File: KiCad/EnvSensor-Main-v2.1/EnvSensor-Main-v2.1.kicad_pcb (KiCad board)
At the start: 4 copper layers, 102 x 100 mm, 90 parts, among them J1 Conn_01x02, J2 Conn_01x02, J3 HPMA115C0-003, J4 Conn_01x02, J5 Micro_SD_Card_Det, J6 SWD, J7 I2C, J8 POWER_INPUT, Q1 Si3407DV, Q2 IRLML2502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

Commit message: Finishing touches
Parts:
- moved JP4 2.87 mm to (40.6, 81.1)
- moved J4 1.65 mm to (38.1, 79.7)
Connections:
- net Net-(J2-Pin_1) renamed /SCD_POWER
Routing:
- net +3V3: track 327.9 -> 320.2 mm, vias 17 -> 15
- net SDIO_CLK: track 47.9 -> 49.4 mm
- net WIFI_ENABLE: track 69.8 -> 68.9 mm
- net Net-(R10-Pad2): track 72.9 -> 72.3 mm
- net POWER_5V_ENABLE: track 94.6 -> 95.2 mm
- net SDIO_DATA0: track 35.7 -> 35.1 mm
- net GND: vias 77 -> 79

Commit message: More fixes
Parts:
- C25: footprint Capacitor_SMD:CP_Elec_6.3x5.8 -> Capacitor_SMD:CP_Elec_4x5.3
- J7: footprint Connector_PinSocket_2.54mm:PinSocket_1x04_P2.54mm_Vertical -> Connector_PinSocket_2.54mm:PinSocket_1x04_P2.54mm_Horizontal; moved to B.Cu
- moved D3 17.0 mm to (106.8, 111.7)
- moved D4 17.0 mm to (108.0, 110.0)
- moved R19 17.0 mm to (106.8, 107.7)
- moved D7 11.2 mm to (98.8, 111.8)
- moved D8 11.2 mm to (100.0, 110.0)
- moved R21 11.2 mm to (98.8, 107.8)
- moved D1 9.50 mm to (90.8, 111.7)
- moved D2 9.50 mm to (92.0, 110.0)
- moved R18 9.50 mm to (90.8, 107.7)
- moved D5 6.95 mm to (82.7, 111.7)
- moved D6 6.95 mm to (84.0, 110.0)
- moved R20 6.95 mm to (82.8, 107.7)
- moved J7 5.65 mm to (80.9, 29.4), turned to -90 degrees
- moved J8 1.69 mm to (111.0, 115.0)
- moved U7 1.22 mm to (19.5, 107.5)
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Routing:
- net LED_2: track 90.1 -> 107.4 mm
- net LED_1: track 87.1 -> 94.7 mm
- net SDA: track 156.5 -> 150.9 mm
- net SCL: track 153.3 -> 147.8 mm
- net LED_4: track 97.4 -> 101.3 mm
- net LED_3: track 94.4 -> 91.0 mm
- net +5V: track 148.0 -> 149.9 mm
- net POWER_5V_ENABLE: track 95.2 -> 96.7 mm
- net GND: track 149.2 -> 148.1 mm, vias 79 -> 80
- net +3V3: track 320.2 -> 319.5 mm
- net E_INK_SELECT: track 27.5 -> 28.1 mm
- net E_INK_RESET: track 29.2 -> 29.7 mm
- net E_INK_BUSY: track 30.1 -> 30.6 mm
- net SCK: track 27.1 -> 27.6 mm
- net E_INK_DC: track 28.4 -> 28.9 mm

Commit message: More fixes
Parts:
- added H5: MountingHole, TestPoint:TestPoint_THTPad_D1.5mm_Drill0.7mm, F.Cu at (78.8, 23.6)
- added H6: MountingHole, TestPoint:TestPoint_THTPad_D1.5mm_Drill0.7mm, F.Cu at (92.8, 23.6)
- J7: moved to F.Cu
- L1: footprint Inductor_SMD:L_1206_3216Metric -> Inductor_SMD:L_1210_3225Metric
- Q1: footprint Package_TO_SOT_SMD:TSOT-23-6 -> Package_TO_SOT_SMD:TSOT-23-6_HandSoldering
- Q2: footprint Package_TO_SOT_SMD:SOT-23 -> Package_TO_SOT_SMD:SOT-23-3
- SW1: footprint Button_Switch_THT:SW_Tactile_SKHH_Angled -> Button_Switch_THT:SW_Tactile_SPST_Angled_PTS645Vx83-2LFS
- moved J7 8.80 mm to (89.6, 28.4)
- moved J5 3.29 mm to (28.5, 93.0)
- moved D2 2.28 mm to (92.0, 112.3), turned to 90 degrees
- moved D8 2.28 mm to (100.0, 112.3), turned to 90 degrees
- moved D4 2.20 mm to (108.0, 112.2), turned to 90 degrees
- moved D6 2.20 mm to (84.0, 112.2), turned to 90 degrees
- moved SW1 1.83 mm to (21.7, 46.1)
- moved D1 1.53 mm to (89.6, 110.8), turned to 90 degrees
- moved D7 1.49 mm to (97.6, 110.8), turned to 90 degrees
- moved D3 1.47 mm to (105.6, 110.8), turned to 90 degrees
- moved D5 1.42 mm to (81.6, 110.8), turned to 90 degrees
- moved R21 1.20 mm to (99.1, 106.6), turned to 0 degrees
- moved R18 1.17 mm to (91.1, 106.6), turned to 0 degrees
- moved R19 1.16 mm to (107.1, 106.6), turned to 0 degrees
- moved R20 1.16 mm to (83.1, 106.6), turned to 0 degrees
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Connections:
- D1 pad 1: Net-(D1-K) -> GND
- D1 pad 2: LED_1 -> Net-(D1-A)
- D2 pad 1: Net-(D1-K) -> GND
- D2 pad 2: LED_1 -> Net-(D1-A)
- D3 pad 1: Net-(D3-K) -> GND
- D3 pad 2: LED_2 -> Net-(D3-A)
- D4 pad 1: Net-(D3-K) -> GND
- D4 pad 2: LED_2 -> Net-(D3-A)
- D5 pad 1: Net-(D5-K) -> GND
- D5 pad 2: LED_3 -> Net-(D5-A)
- D6 pad 1: Net-(D5-K) -> GND
- D6 pad 2: LED_3 -> Net-(D5-A)
- D7 pad 1: Net-(D7-K) -> GND
- D7 pad 2: LED_4 -> Net-(D7-A)
- D8 pad 1: Net-(D7-K) -> GND
- D8 pad 2: LED_4 -> Net-(D7-A)
- R18 pad 1: Net-(D1-K) -> LED_1
- R18 pad 2: GND -> Net-(D1-A)
- R19 pad 1: Net-(D3-K) -> LED_2
- R19 pad 2: GND -> Net-(D3-A)
- R20 pad 1: Net-(D5-K) -> LED_3
- R20 pad 2: GND -> Net-(D5-A)
- R21 pad 1: Net-(D7-K) -> LED_4
- R21 pad 2: GND -> Net-(D7-A)
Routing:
- net +3V3: track 319.5 -> 300.2 mm
- net GND: track 148.1 -> 157.8 mm, vias 80 -> 76
- net LED_3: track 91.0 -> 83.2 mm
- net LED_1: track 94.7 -> 88.6 mm
- net LED_4: track 101.3 -> 95.4 mm
- net Net-(D7-A): track 0.00 -> 5.59 mm
- net Net-(D1-A): track 0.00 -> 5.59 mm
- net Net-(D5-A): track 0.00 -> 5.54 mm
- net Net-(D3-A): track 0.00 -> 5.54 mm
- net LED_2: track 107.4 -> 102.2 mm
- net Net-(D5-K): track 4.30 -> 0.00 mm
- net Net-(D7-K): track 4.27 -> 0.00 mm
- net Net-(D3-K): track 4.27 -> 0.00 mm
- net Net-(D1-K): track 4.24 -> 0.00 mm
- net POWER_5V_ENABLE: track 96.7 -> 100.0 mm
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
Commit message: More work
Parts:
- J1, J2, J4: footprint Connector_PinHeader_2.54mm:PinHeader_1x02_P2.54mm_Vertical -> Connector_PinHeader_2.54mm:PinHeader_1x02_P2.54mm_Horizontal
- moved R9 19.4 mm to (64.8, 68.2), turned to 0 degrees
- moved R8 17.8 mm to (69.1, 68.0), turned to 180 degrees
- moved JP4 7.77 mm to (33.4, 83.8), turned to 0 degrees
- moved J4 6.27 mm to (32.1, 81.4), turned to 90 degrees
- moved JP2 4.01 mm to (93.2, 47.0), turned to 180 degrees
- moved R3 3.30 mm to (41.1, 86.5)
- moved R4 3.30 mm to (41.1, 88.5)
- moved C14 3.30 mm to (40.0, 91.3)
- moved C15 3.30 mm to (41.7, 91.2)
- moved Q1 3.30 mm to (41.0, 83.2)
- moved R2 3.30 mm to (41.0, 80.5)
- moved R5 3.30 mm to (43.0, 95.8)
- moved R6 3.30 mm to (41.0, 96.6)
- moved R7 3.30 mm to (39.0, 97.2)
- moved L1 0.45 mm to (44.2, 46.6)
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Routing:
- net +3V3: track 300.2 -> 314.2 mm, vias 15 -> 14
- net SCL: track 147.8 -> 155.9 mm
- net SDIO_DETECT: track 40.3 -> 36.7 mm
- net SDIO_POWER_ENABLE: track 32.3 -> 29.1 mm
- net +3.3VA: track 5.02 -> 7.91 mm
- net Net-(J4-Pin_2): track 7.33 -> 9.22 mm
- net SDIO_DATA1: track 33.2 -> 34.6 mm
- net SDIO_DATA0: track 35.1 -> 36.5 mm
- net POWER_5V_ENABLE: track 100.0 -> 98.6 mm
- net LED_3: track 83.2 -> 82.1 mm
- net LED_1: track 88.6 -> 87.5 mm
- net SDIO_CMD: track 55.4 -> 54.5 mm
- net SDIO_DATA3: track 52.1 -> 51.2 mm
- net LED_4: track 95.4 -> 94.6 mm
- net LED_2: track 102.2 -> 101.4 mm
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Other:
- board text added: "5V En"
- board text added: "NRST"
- board text added: "SWCLK"
- board text added: "SWDIO"
- board text added: "SWO"
- board text removed: "5V Enable"

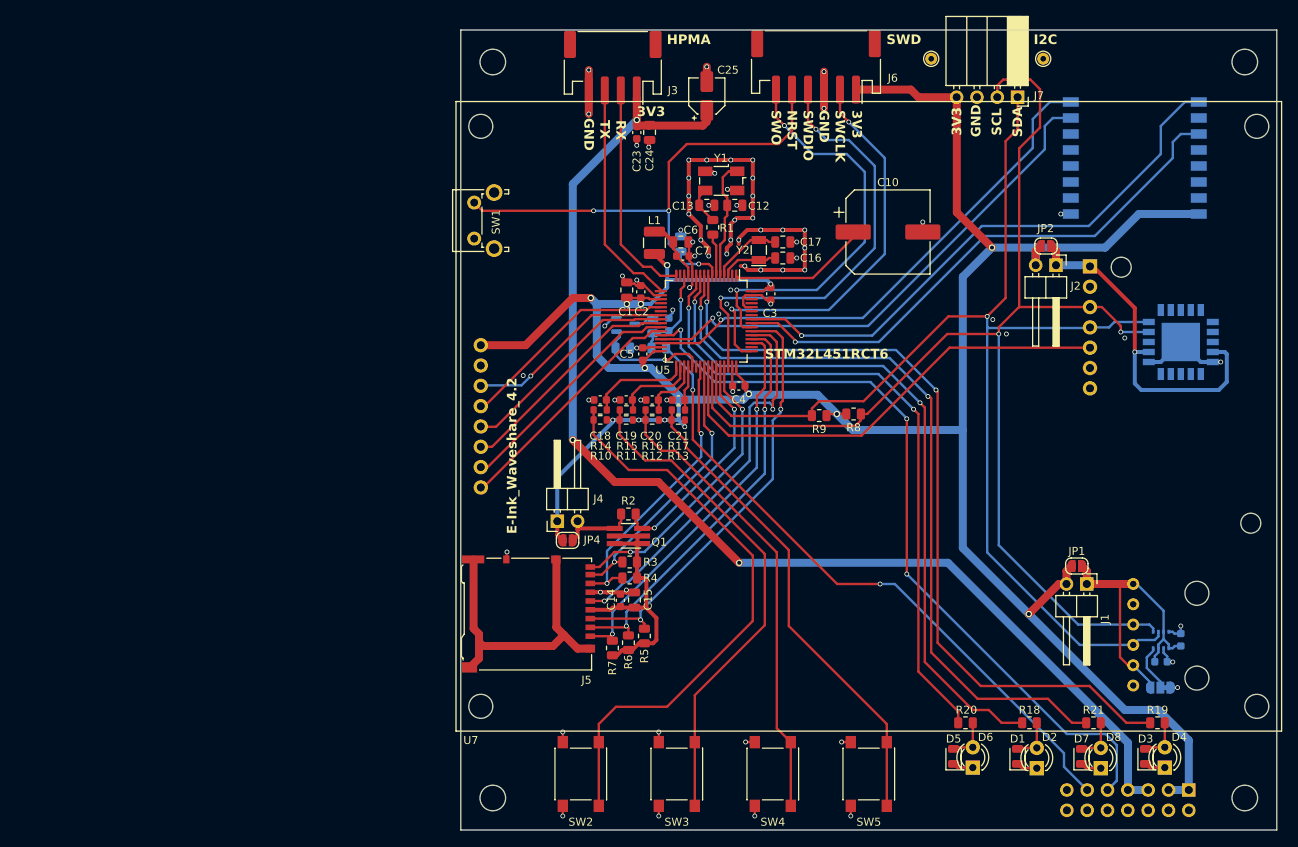
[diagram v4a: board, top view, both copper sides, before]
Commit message: Bore moving swd and i2c
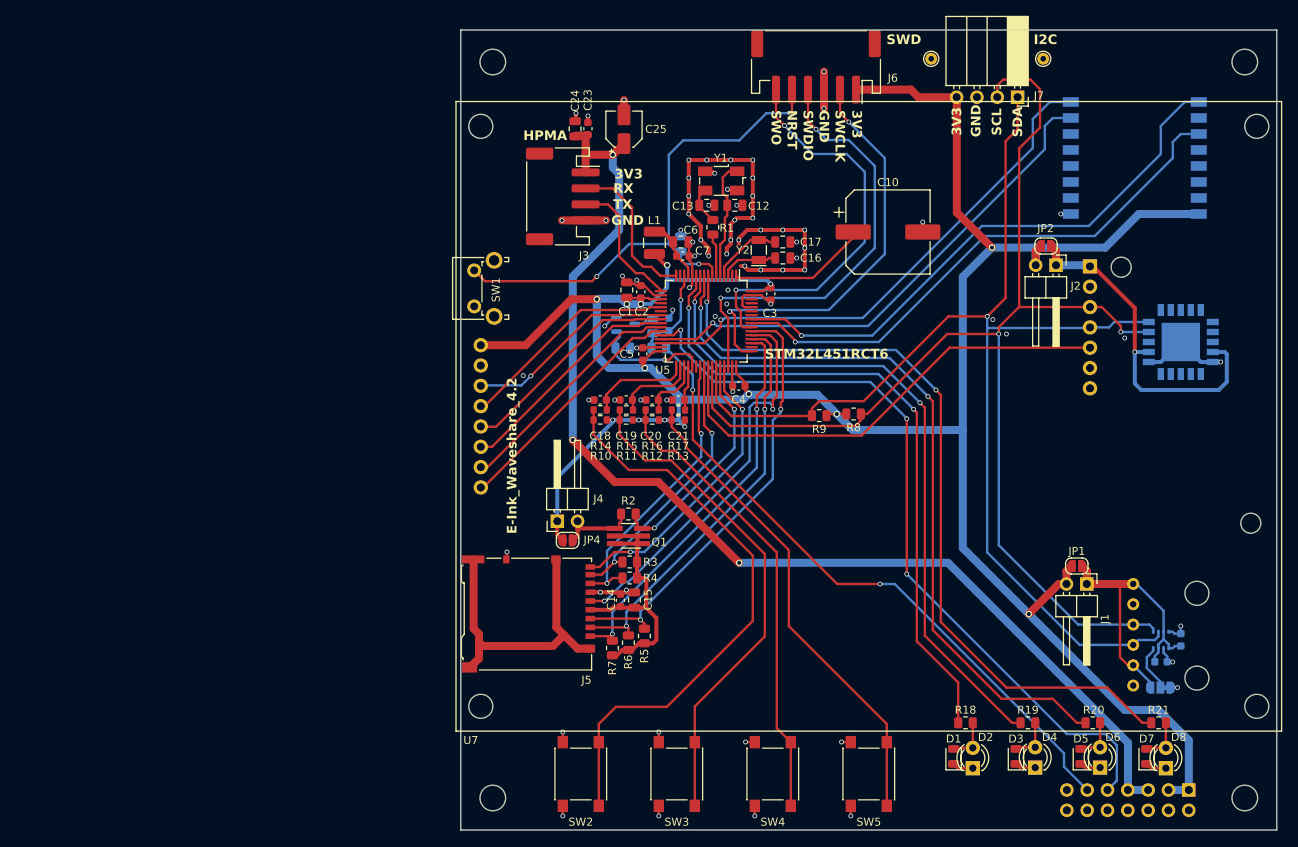
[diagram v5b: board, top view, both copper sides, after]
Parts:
- moved J3 17.3 mm to (32.8, 40.8), turned to -90 degrees
- moved D4 16.2 mm to (91.8, 112.2)
- moved R19 16.2 mm to (90.9, 106.6)
- moved D3 16.2 mm to (89.4, 110.8)
- moved D5 15.9 mm to (97.5, 110.8)
- moved D6 15.9 mm to (99.9, 112.2)
- moved R20 15.9 mm to (99.0, 106.6)
- moved C25 11.2 mm to (40.4, 32.4)
- moved C24 9.32 mm to (34.3, 32.4), turned to 90 degrees
- moved SW1 8.47 mm to (21.7, 54.5)
- moved D7 8.14 mm to (105.7, 110.8)
- moved D8 8.14 mm to (108.1, 112.3)
- moved R21 8.14 mm to (107.2, 106.6)
- moved D1 8.00 mm to (81.6, 110.8)
- moved D2 8.00 mm to (84.0, 112.3)
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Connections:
- U5 pad 10: LED_1 -> LED_2
- U5 pad 11: LED_3 -> LED_1
- U5 pad 8: LED_2 -> LED_4
- U5 pad 9: LED_4 -> LED_3
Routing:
- net LED_2: track 101.4 -> 85.6 mm
- net HPMA_TX: track 27.8 -> 16.9 mm
- net LED_3: track 82.1 -> 92.7 mm
- net HPMA_RX: track 27.4 -> 19.9 mm
- net +5V: track 149.9 -> 143.4 mm
- net LED_1: track 87.5 -> 82.1 mm
- net LED_4: track 94.6 -> 99.7 mm
- net NRST: track 64.5 -> 66.6 mm
- net WIFI_RX: track 65.5 -> 64.8 mm

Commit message: Before moving i2c tracks
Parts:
- J6: moved to B.Cu
- J7: footprint Connector_PinSocket_2.54mm:PinSocket_1x04_P2.54mm_Horizontal -> JPConnectors:PinSocket_1x04_P2.54mm_Horizontal_SMD
- moved H5 95.9 mm to (25.0, 103.0), turned to 90 degrees
- moved H6 90.7 mm to (25.0, 83.8), turned to 90 degrees
- moved J7 85.1 mm to (30.4, 89.6), turned to 0 degrees
- moved J6 79.7 mm to (24.0, 93.3), turned to 90 degrees
- moved J5 46.4 mm to (73.3, 80.8), turned to 90 degrees
- moved R8 46.1 mm to (114.8, 73.8)
- moved R9 44.9 mm to (109.4, 73.2)
- moved J4 39.2 mm to (69.7, 92.4), turned to -90 degrees
- moved JP4 35.6 mm to (68.4, 90.0), turned to 180 degrees
- moved R7 31.6 mm to (62.8, 76.5), turned to 90 degrees
- moved R6 27.7 mm to (60.8, 77.2), turned to 90 degrees
- moved R5 23.8 mm to (58.8, 78.0), turned to 90 degrees
- moved R2 23.6 mm to (60.8, 93.3), turned to 180 degrees
- moved C14 23.6 mm to (61.8, 82.5), turned to 90 degrees
- moved Q1 21.1 mm to (60.8, 90.5), turned to 0 degrees
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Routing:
- net POWER_5V_ENABLE: track 98.6 -> 35.9 mm, vias 3 -> 1
- net +5V: track 143.4 -> 87.8 mm, vias 3 -> 1
- net +3V3: track 314.6 -> 268.1 mm, vias 14 -> 12
- net LED_4: track 99.7 -> 65.1 mm
- net LED_3: track 92.7 -> 58.2 mm
- net SWO: track 49.8 -> 84.1 mm, vias 2 -> 1
- net LED_2: track 85.6 -> 54.3 mm
- net LED_1: track 82.1 -> 52.9 mm
- net NRST: track 66.6 -> 91.7 mm, vias 3 -> 5
- net SWCLK: track 51.2 -> 75.7 mm, vias 2 -> 1
- net SDIO_POWER_ENABLE: track 29.1 -> 51.0 mm
- net SWDIO: track 54.7 -> 74.0 mm, vias 2 -> 1
- net SDA: track 150.9 -> 170.1 mm
- net +BATT: track 81.8 -> 100.7 mm
- net E_INK_BUSY: track 30.6 -> 46.7 mm
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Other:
- board text added: "MicroSD"

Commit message: Finish
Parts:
- added JP5: NC, Jumper:SolderJumper-2_P1.3mm_Bridged_RoundedPad1.0x1.5mm, F.Cu at (78.8, 110.8)
- C1: footprint Capacitor_SMD:C_0805_2012Metric -> Jumper:SolderJumper-2_P1.3mm_Bridged_RoundedPad1.0x1.5mm
- JP4, R8, R9: moved to B.Cu
- Q1: footprint Package_TO_SOT_SMD:TSOT-23-6_HandSoldering -> Package_TO_SOT_SMD:TSOT-23-6
- moved R8 58.3 mm to (58.0, 60.6)
- moved R9 57.2 mm to (53.8, 59.8)
- moved J7 5.18 mm to (25.8, 87.3)
- moved JP1 4.40 mm to (97.0, 91.4)
- moved H5 3.62 mm to (22.2, 100.7)
- moved H6 3.62 mm to (22.2, 81.5)
- moved JP4 3.41 mm to (66.4, 92.8), turned to 90 degrees
- moved J6 2.72 mm to (22.6, 91.0)
- moved R4 2.66 mm to (59.8, 87.8), turned to -90 degrees
- moved R5 2.62 mm to (60.9, 79.6), turned to 180 degrees
- moved J1 2.53 mm to (95.7, 89.2), turned to 90 degrees
- moved R7 2.12 mm to (60.9, 75.6), turned to 180 degrees
- moved C18 1.37 mm to (45.5, 54.4)
- moved C19 1.37 mm to (48.7, 54.4)
- moved C20 1.37 mm to (52.0, 54.4)
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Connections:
- D1 pad 1: GND -> Net-(D1-K)
- D3 pad 1: GND -> Net-(D1-K)
- D5 pad 1: GND -> Net-(D1-K)
- D7 pad 1: GND -> Net-(D1-K)
- J1 pad 1: /BMP280_VCC -> +3V3
- J1 pad 2: +3V3 -> /BMP280_VCC
- J4 pad 1: +3V3 -> Net-(J4-Pin_1)
- J4 pad 2: Net-(J4-Pin_2) -> +3V3
- JP4 pad 2: Net-(J4-Pin_2) -> Net-(J4-Pin_1)
- Q1 pad 4: Net-(J4-Pin_2) -> Net-(J4-Pin_1)
- R2 pad 1: Net-(J4-Pin_2) -> Net-(J4-Pin_1)
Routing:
- net +3V3: track 268.1 -> 361.8 mm, vias 12 -> 13
- net POWER_5V_ENABLE: track 35.9 -> 106.7 mm, vias 1 -> 2
- net +5V: track 87.8 -> 145.7 mm, vias 1 -> 3
- net Net-(D1-K): track 0.00 -> 46.7 mm, vias 0 -> 2
- net LED_1: track 52.9 -> 86.6 mm
- net LED_4: track 65.1 -> 98.4 mm
- net LED_3: track 58.2 -> 91.4 mm
- net LED_2: track 54.3 -> 87.0 mm
- net SDA: track 170.1 -> 157.9 mm, vias 1 -> 3
- net Net-(J4-Pin_1): track 0.00 -> 11.3 mm
- net Net-(J4-Pin_2): track 9.22 -> 0.00 mm
- net Net-(R10-Pad2): track 65.0 -> 72.0 mm, vias 2 -> 0
- net +BATT: track 100.7 -> 106.9 mm, vias 2 -> 1
- net SCL: track 164.4 -> 158.3 mm
- net SDIO_DATA0: track 41.0 -> 46.8 mm, vias 2 -> 0
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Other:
- board text added: "EnvSensor 2.1 Main Board JP, 22.07.2024 Wrocław"

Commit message: c++ project for 2.1 introduced
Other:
- board text added: "Bugs: 1. Recompute areas 2. C1 - wrong footprint"
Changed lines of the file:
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@@
     (effects (font (size 1.2 1.2) (thickness 0.2) bold) (justify left))
+  )
+  (gr_text "Bugs:\n1. Recompute areas\n2. C1 - wrong footprint" (at -35.6 46.2) (layer "F.SilkS")
+    (effects (font (size 1.5 1.5) (thickness 0.3) bold) (justify left top))
   )
   (gr_text "GND" (at 29.2 92.5) (layer "F.SilkS")
